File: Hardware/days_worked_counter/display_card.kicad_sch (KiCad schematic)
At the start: 2 parts, among them U501 SN74HC595

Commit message: Cleanup more stuff
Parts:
- added Q501: MMBT3904, Package_TO_SOT_SMD:SOT-23, symbol Transistor_BJT:MMBT3904
- added R501: 10K, Resistor_SMD:R_0805_2012Metric, symbol Device:R_Small
- added R?: 750R?, Resistor_SMD:R_0805_2012Metric, symbol Device:R_Small
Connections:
- net GND: now also Q501.2 (E), R501.2
- net SEG_B: now reaches U501.1 (QB)
- net SEG_A: now reaches U501.15 (QA)
- net SEG_A: now also Q501.1 (B), R501.1
- net SEG_C: now reaches U501.2 (QC)
- net SEG_D: now reaches U501.3 (QD)
- net SEG_E: now reaches U501.4 (QE)
- net SEG_F: now reaches U501.5 (QF)
- net SEG_G: now reaches U501.6 (QG)
- net SEG_H: now reaches U501.7 (QH)
- new net: Q501.3 (C), R?.2
- new net SEG_A_LAMP: R?.1
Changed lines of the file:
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@@
 (kicad_sch (version 20211123) (generator eeschema)
   (paper "A4")
+  (junction (at 185.42 81.28) (diameter 0) (color 0 0 0 0)
+  )
+  (wire (pts (xy 162.56 90.17) (xy 154.94 90.17))
+    (stroke (width 0) (type default) (color 0 0 0 0))
+  )
+  (wire (pts (xy 176.53 81.28) (xy 185.42 81.28))
+    (stroke (width 0) (type default) (color 0 0 0 0))
+  )
+  (wire (pts (xy 162.56 87.63) (xy 154.94 87.63))
+    (stroke (width 0) (type default) (color 0 0 0 0))
+  )
+  (wire (pts (xy 162.56 95.25) (xy 154.94 95.25))
+    (stroke (width 0) (type default) (color 0 0 0 0))
+  )
+  (wire (pts (xy 195.58 67.31) (xy 195.58 69.85))
+    (stroke (width 0) (type default) (color 0 0 0 0))
+  )
   (wire (pts (xy 132.08 72.39) (xy 132.08 73.66))
     (stroke (width 0) (type default) (color 0 0 0 0))
@@
     (stroke (width 0) (type default) (color 0 0 0 0))
   )
+  (wire (pts (xy 162.56 97.79) (xy 154.94 97.79))
+    (stroke (width 0) (type default) (color 0 0 0 0))
+  )
+  (wire (pts (xy 162.56 92.71) (xy 154.94 92.71))
+    (stroke (width 0) (type default) (color 0 0 0 0))
+  )
+  (wire (pts (xy 162.56 105.41) (xy 154.94 105.41))
+    (stroke (width 0) (type default) (color 0 0 0 0))
+  )
   (wire (pts (xy 146.05 111.76) (xy 146.05 113.03))
     (stroke (width 0) (type default) (color 0 0 0 0))
@@
     (stroke (width 0) (type default) (color 0 0 0 0))
   )
+  (wire (pts (xy 185.42 87.63) (xy 185.42 88.9))
+    (stroke (width 0) (type default) (color 0 0 0 0))
+  )
   (wire (pts (xy 114.3 100.33) (xy 137.16 100.33))
     (stroke (width 0) (type default) (color 0 0 0 0))
   )
+  (wire (pts (xy 162.56 100.33) (xy 154.94 100.33))
+    (stroke (width 0) (type default) (color 0 0 0 0))
+  )
   (wire (pts (xy 118.11 92.71) (xy 118.11 93.98))
     (stroke (width 0) (type default) (color 0 0 0 0))
   )
+  (wire (pts (xy 195.58 74.93) (xy 195.58 76.2))
+    (stroke (width 0) (type default) (color 0 0 0 0))
+  )
+  (wire (pts (xy 185.42 81.28) (xy 187.96 81.28))
+    (stroke (width 0) (type default) (color 0 0 0 0))
+  )
   (wire (pts (xy 132.08 90.17) (xy 137.16 90.17))
     (stroke (width 0) (type default) (color 0 0 0 0))
@@
     (stroke (width 0) (type default) (color 0 0 0 0))
   )
+  (wire (pts (xy 162.56 102.87) (xy 154.94 102.87))
+    (stroke (width 0) (type default) (color 0 0 0 0))
+  )
   (wire (pts (xy 163.83 110.49) (xy 172.72 110.49))
     (stroke (width 0) (type default) (color 0 0 0 0))
@@
     (stroke (width 0) (type default) (color 0 0 0 0))
   )
+  (wire (pts (xy 208.28 67.31) (xy 195.58 67.31))
+    (stroke (width 0) (type default) (color 0 0 0 0))
+  )
+  (wire (pts (xy 195.58 86.36) (xy 195.58 88.9))
+    (stroke (width 0) (type default) (color 0 0 0 0))
+  )
   (wire (pts (xy 132.08 97.79) (xy 137.16 97.79))
     (stroke (width 0) (type default) (color 0 0 0 0))
   )
+  (wire (pts (xy 185.42 81.28) (xy 185.42 82.55))
+    (stroke (width 0) (type default) (color 0 0 0 0))
+  )
   (wire (pts (xy 163.83 113.03) (xy 172.72 113.03))
     (stroke (width 0) (type default) (color 0 0 0 0))
@@
   (wire (pts (xy 137.16 92.71) (xy 118.11 92.71))
     (stroke (width 0) (type default) (color 0 0 0 0))
+  )
+  (label "SEG_B" (at 162.56 90.17 180)
+    (effects (font (size 1.27 1.27)) (justify right bottom))
+  )
+  (label "SEG_F" (at 162.56 100.33 180)
+    (effects (font (size 1.27 1.27)) (justify right bottom))
+  )
+  (label "SEG_H" (at 162.56 105.41 180)
+    (effects (font (size 1.27 1.27)) (justify right bottom))
+  )
+  (label "SEG_D" (at 162.56 95.25 180)
+    (effects (font (size 1.27 1.27)) (justify right bottom))
+  )
+  (label "SEG_E" (at 162.56 97.79 180)
+    (effects (font (size 1.27 1.27)) (justify right bottom))
+  )
+  (label "SEG_A" (at 176.53 81.28 0)
+    (effects (font (size 1.27 1.27)) (justify left bottom))
+  )
+  (label "SEG_G" (at 162.56 102.87 180)
+    (effects (font (size 1.27 1.27)) (justify right bottom))
+  )
+  (label "SEG_A_LAMP" (at 208.28 67.31 180)
+    (effects (font (size 1.27 1.27)) (justify right bottom))
+  )
+  (label "SEG_A" (at 162.56 87.63 180)
+    (effects (font (size 1.27 1.27)) (justify right bottom))
+  )
+  (label "SEG_C" (at 162.56 92.71 180)
+    (effects (font (size 1.27 1.27)) (justify right bottom))
   )
   (hierarchical_label "DATA_IN" (shape input) (at 132.08 90.17 180)
@@
   (hierarchical_label "LATCH_OUT" (shape output) (at 172.72 110.49 0)
     (effects (font (size 1.27 1.27)) (justify left))
+  )
+  (symbol (lib_id "Transistor_BJT:MMBT3904") (at 193.04 81.28 0) (unit 1)
+    (in_bom yes) (on_board yes) (fields_autoplaced)
+    (property "Reference" "Q501" (id 0) (at 198.12 80.0099 0)
+      (effects (font (size 1.27 1.27)) (justify left))
+    )
+    (property "Value" "MMBT3904" (id 1) (at 198.12 82.5499 0)
+      (effects (font (size 1.27 1.27)) (justify left))
+    )
+    (property "Footprint" "Package_TO_SOT_SMD:SOT-23" (id 2) (at 198.12 83.185 0)
+      (effects (font (size 1.27 1.27) italic) (justify left) hide)
+    )
+    (property "Datasheet" "https://www.onsemi.com/pub/Collateral/2N3903-D.PDF" (id 3) (at 193.04 81.28 0)
+      (effects (font (size 1.27 1.27)) (justify left) hide)
+    )
+    (pin "1")
+    (pin "2")
+    (pin "3")
+  )
+  (symbol (lib_id "power:GND") (at 185.42 88.9 0) (unit 1)
+    (in_bom yes) (on_board yes)
+    (property "Reference" "#PWR0144" (id 0) (at 185.42 95.25 0)
+      (effects (font (size 1.27 1.27)) hide)
+    )
+    (property "Value" "GND" (id 1) (at 185.42 92.71 0))
+    (property "Footprint" "" (id 2) (at 185.42 88.9 0)
+      (effects (font (size 1.27 1.27)) hide)
+    )
+    (property "Datasheet" "" (id 3) (at 185.42 88.9 0)
+      (effects (font (size 1.27 1.27)) hide)
+    )
+    (pin "1")
   )
   (symbol (lib_id "Device:C_Small") (at 132.08 76.2 0) (unit 1)
@@
   (symbol (lib_id "KenwoodFox:SN74HC595") (at 146.05 92.71 0) (unit 1)
     (in_bom yes) (on_board yes)
-    (property "Reference" "U501" (id 0) (at 139.7 83.82 0)
+    (property "Reference" "U501" (id 0) (at 138.43 83.82 0)
       (effects (font (size 1.27 1.27)) (justify left))
     )
@@
     (pin "1")
   )
+  (symbol (lib_id "Device:R_Small") (at 195.58 72.39 0) (unit 1)
+    (in_bom yes) (on_board yes)
+    (property "Reference" "R?" (id 0) (at 191.77 71.12 0))
+    (property "Value" "750R?" (id 1) (at 191.77 73.66 0))
+    (property "Footprint" "Resistor_SMD:R_0805_2012Metric" (id 2) (at 195.58 72.39 0)
+      (effects (font (size 1.27 1.27)) hide)
+    )
+    (property "Datasheet" "~" (id 3) (at 195.58 72.39 0)
+      (effects (font (size 1.27 1.27)) hide)
+    )
+    (pin "1")
+    (pin "2")
+  )
   (symbol (lib_id "power:+5V") (at 114.3 99.06 0) (unit 1)
     (in_bom yes) (on_board yes)
@@
     (pin "1")
   )
+  (symbol (lib_id "Device:R_Small") (at 185.42 85.09 0) (unit 1)
+    (in_bom yes) (on_board yes)
+    (property "Reference" "R501" (id 0) (at 181.61 83.82 0))
+    (property "Value" "10K" (id 1) (at 181.61 86.36 0))
+    (property "Footprint" "Resistor_SMD:R_0805_2012Metric" (id 2) (at 185.42 85.09 0)
+      (effects (font (size 1.27 1.27)) hide)
+    )
+    (property "Datasheet" "~" (id 3) (at 185.42 85.09 0)
+      (effects (font (size 1.27 1.27)) hide)
+    )
+    (pin "1")
+    (pin "2")
+  )
   (symbol (lib_id "power:GND") (at 118.11 93.98 0) (unit 1)
     (in_bom yes) (on_board yes)
@@
       (effects (font (size 1.27 1.27)) hide)
     )
+    (pin "1")
+  )
+  (symbol (lib_id "power:GND") (at 195.58 88.9 0) (unit 1)
+    (in_bom yes) (on_board yes)
+    (property "Reference" "#PWR0145" (id 0) (at 195.58 95.25 0)
+      (effects (font (size 1.27 1.27)) hide)
+    )
+    (property "Value" "GND" (id 1) (at 195.58 92.71 0))
+    (property "Footprint" "" (id 2) (at 195.58 88.9 0)
+      (effects (font (size 1.27 1.27)) hide)
+    )
+    (property "Datasheet" "" (id 3) (at 195.58 88.9 0)
+      (effects (font (size 1.27 1.27)) hide)
+    )

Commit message: Add all the cool stuff
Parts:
- added J501, J502: Conn_01x09, symbol Connector_Generic:Conn_01x09
- added Q502, Q503, Q504, Q505, Q506, Q507, Q508: MMBT3904, Package_TO_SOT_SMD:SOT-23, symbol Transistor_BJT:MMBT3904
- added R502, R503, R504, R505, R510, R511, R512: 10K, Resistor_SMD:R_0805_2012Metric, symbol Device:R_Small
- added R506, R507, R508, R509, R514, R515, R516: 750R?, Resistor_SMD:R_0805_2012Metric, symbol Device:R_Small
- gave numbers to parts that had none: 1
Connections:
- net GND: now also J501.9 (Pin_9), Q502.2 (E), Q503.2 (E), Q504.2 (E), Q505.2 (E), Q506.2 (E), Q507.2 (E), Q508.2 (E), R502.2, R503.2, R504.2, R505.2, R510.2, R511.2, R512.2
- net SEG_A: now also Q502.1 (B), R502.1; no longer Q501.1 (B), R501.1
- net SEG_A_LAMP: now also J502.3 (Pin_3), R506.1; no longer R513.1
- net SEG_B: now also Q501.1 (B), R501.1
- net SEG_C: now also Q503.1 (B), R503.1
- net SEG_D: now also Q506.1 (B), R510.1
- net SEG_E: now also Q504.1 (B), R504.1
- net SEG_F: now also Q507.1 (B), R511.1
- net SEG_G: now also Q505.1 (B), R505.1
- net SEG_H: now also Q508.1 (B), R512.1
- new net: Q504.3 (C), R508.2
- new net: Q506.3 (C), R514.2
- new net: Q507.3 (C), R515.2
- new net: Q503.3 (C), R507.2
- new net: Q505.3 (C), R509.2
- new net: Q502.3 (C), R506.2
- new net: Q508.3 (C), R516.2
- new net +12V: J502.1 (Pin_1)
- new net SEG_B_LAMP: J502.5 (Pin_5), R513.1
- new net SEG_C_LAMP: J502.7 (Pin_7), R507.1
- new net SEG_D_LAMP: J502.9 (Pin_9), R514.1
- new net SEG_E_LAMP: J501.1 (Pin_1), R508.1
- new net SEG_F_LAMP: J501.3 (Pin_3), R515.1
- new net SEG_G_LAMP: J501.5 (Pin_5), R509.1
- new net SEG_H_LAMP: J501.7 (Pin_7), R516.1
- no-connect marks 0 -> 8
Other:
- company: (none) -> FRC 1721
- title: (none) -> Days Without Incident Sign
- moved on the sheet: Q501, R501, R513

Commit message: Even more stuff
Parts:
- J501, J502: footprint (none) -> Connector_PinSocket_2.54mm:PinSocket_1x09_P2.54mm_Vertical
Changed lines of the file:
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@@
       (effects (font (size 1.27 1.27)) (justify left))
     )
-    (property "Footprint" "" (id 2) (at 143.51 137.16 0)
+    (property "Footprint" "Connector_PinSocket_2.54mm:PinSocket_1x09_P2.54mm_Vertical" (id 2) (at 143.51 137.16 0)
       (effects (font (size 1.27 1.27)) hide)
     )
@@
       (effects (font (size 1.27 1.27)) (justify left))
     )
-    (property "Footprint" "" (id 2) (at 180.34 137.16 0)
-      (effects (font (size 1.27 1.27)) hide)
-    )
+    (property "Footprint" "Connector_PinSocket_2.54mm:PinSocket_1x09_P2.54mm_Vertical" (id 2) (at 180.34 137.16 0)
+      (effects (font (size 1.27 1.27)) hide)
+    )

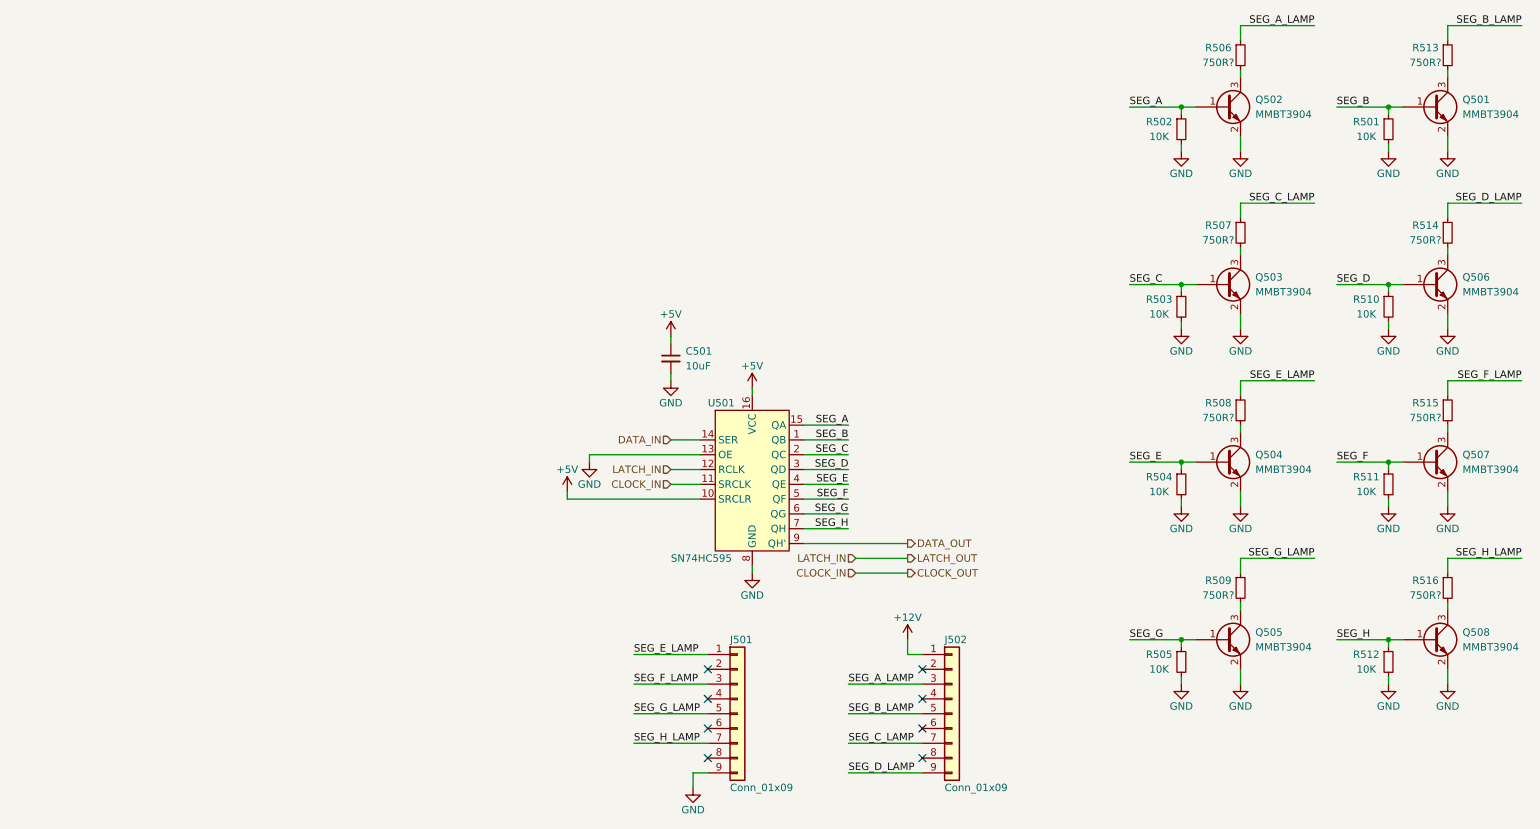
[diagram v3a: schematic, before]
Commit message: Add drawings and pin placements
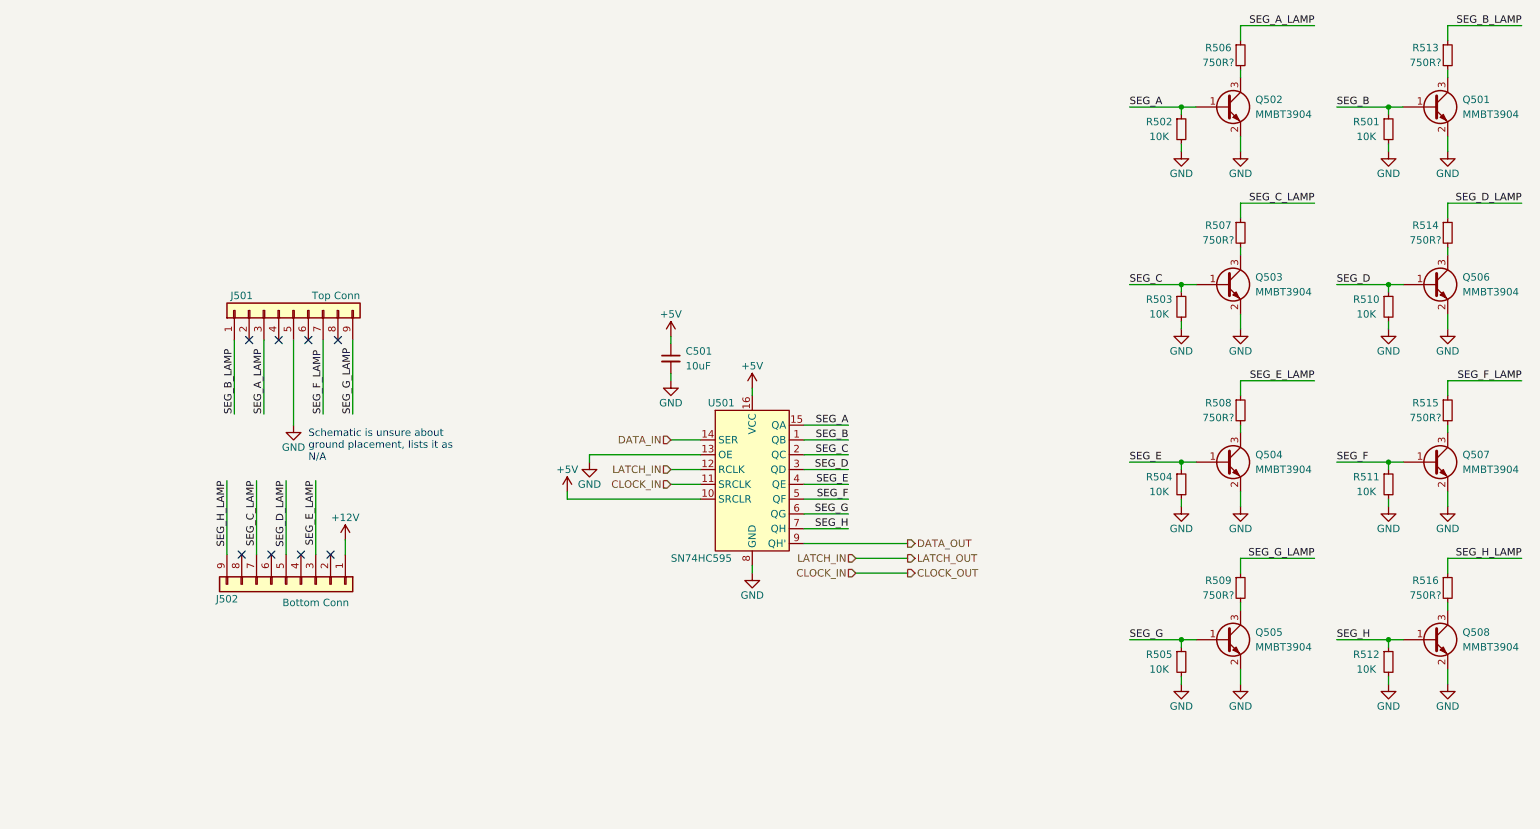
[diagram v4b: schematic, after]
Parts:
- J501: value Conn_01x09 -> Top Conn
- J502: value Conn_01x09 -> Bottom Conn
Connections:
- net GND: now also J501.5 (Pin_5); no longer J501.9 (Pin_9)
- net SEG_A_LAMP: now also J501.3 (Pin_3); no longer J502.3 (Pin_3)
- net SEG_B_LAMP: now also J501.1 (Pin_1); no longer J502.5 (Pin_5)
- net SEG_D_LAMP: now also J502.5 (Pin_5); no longer J502.9 (Pin_9)
- net SEG_E_LAMP: now also J502.3 (Pin_3); no longer J501.1 (Pin_1)
- net SEG_F_LAMP: now also J501.7 (Pin_7); no longer J501.3 (Pin_3)
- net SEG_G_LAMP: now also J501.9 (Pin_9); no longer J501.5 (Pin_5)
- net SEG_H_LAMP: now also J502.9 (Pin_9); no longer J501.7 (Pin_7)
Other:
- note added: "Schematic is unsure about ground placement, lists it as N/A"
- moved on the sheet: J501, J502
